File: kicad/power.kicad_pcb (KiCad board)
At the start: 2 copper layers, 84.1 x 61.7 mm, 10 parts, among them J1 Bus_PCI_Express_x1, J6 USB_C_Receptacle_USB2.0_16P, U1 MP2672GD-0000-Z, U3 MP2236CGJ-Z, U301 MR30-Vertical, U302 MP2236CGJ-Z

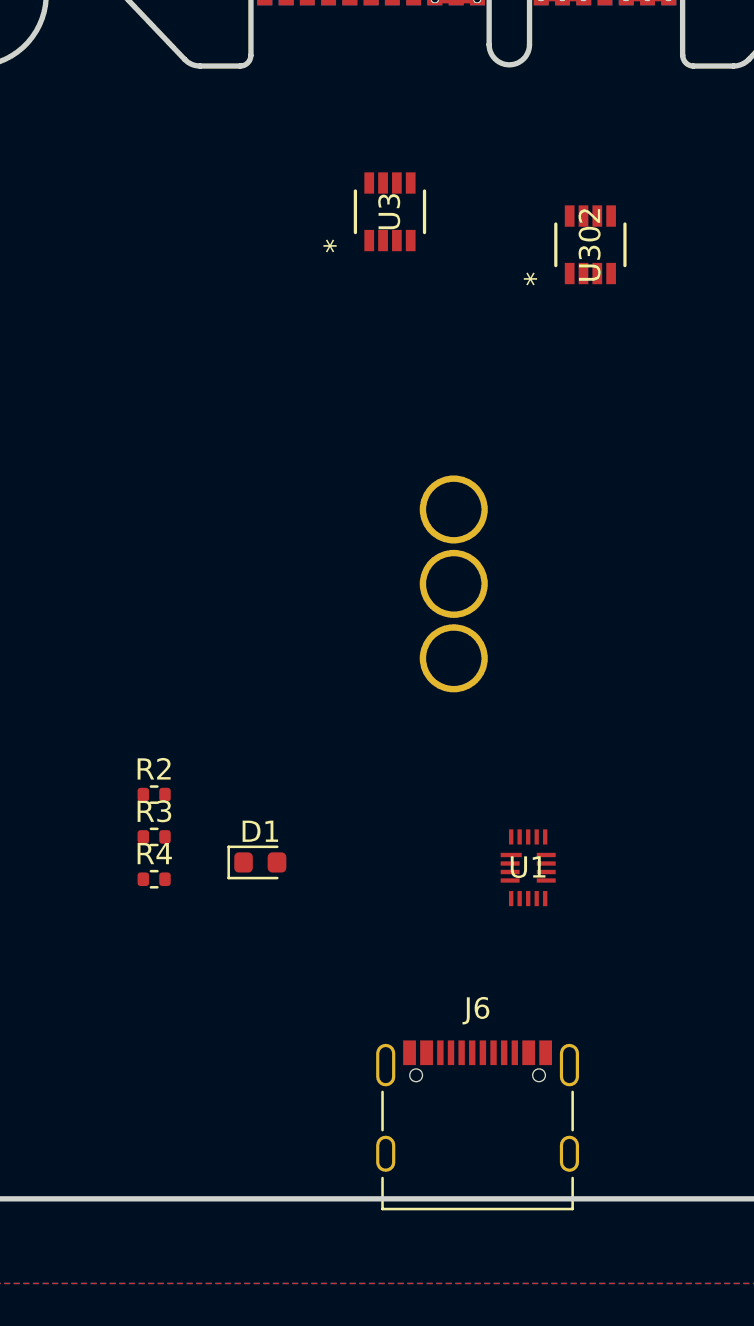
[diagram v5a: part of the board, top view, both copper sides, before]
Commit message: add LCSC PNs and footprints for various components, import custom step file for inductor
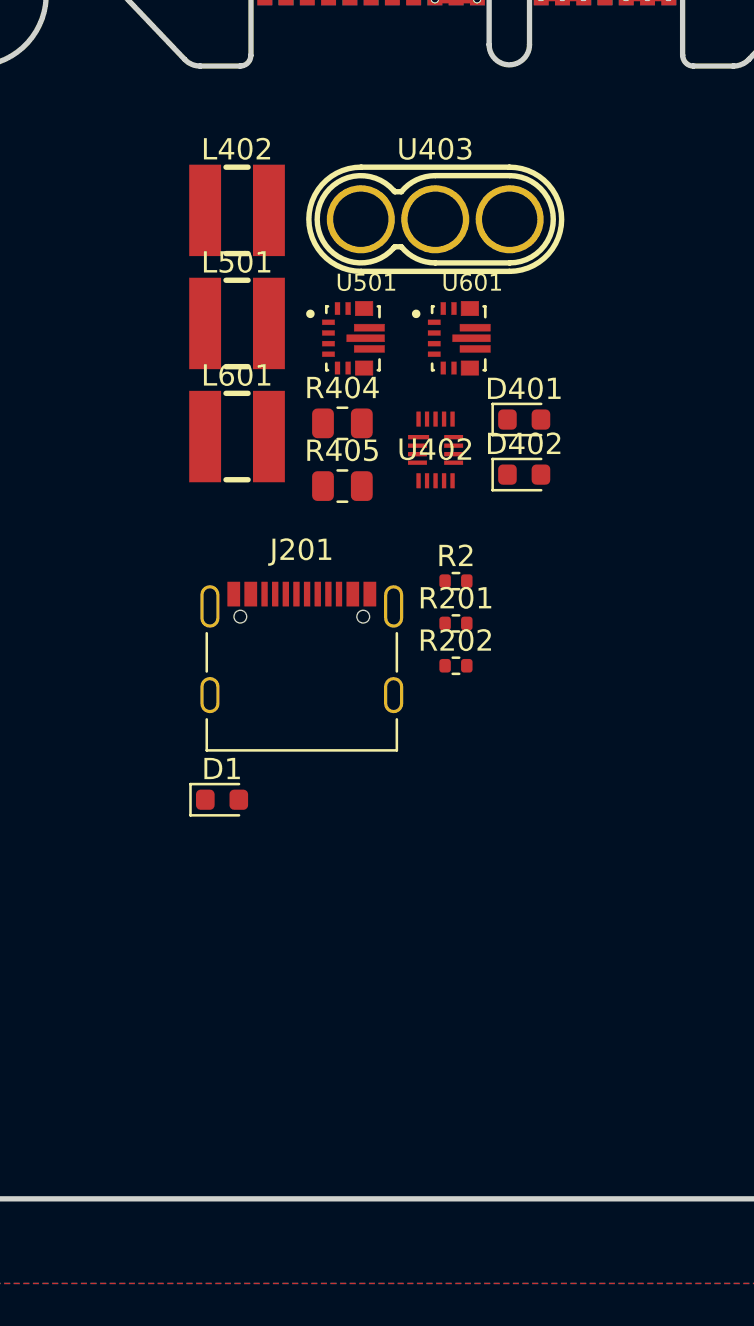
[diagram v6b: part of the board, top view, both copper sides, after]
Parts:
- removed J6: USB_C_Receptacle_USB2.0_16P, Connector_USB:USB_C_Receptacle_Palconn_UTC16-G
- removed R3, R4: 5.1k, Resistor_SMD:R_0402_1005Metric
- removed U1: MP2672GD-0000-Z, 4in-power:QFN-18_2MMx3MM_MP2672_MNP_MPS
- removed U3, U302: MP2236CGJ-Z, 4in-power:TSOT23-8_MP2236C_MNP
- removed U301: MR30-Vertical, 4in-power:CONN-TH_MR30-Vertical
- added D401: LED, LED_SMD:LED_0603_1608Metric, F.Cu at (149.1, 85.8)
- added D402: LED, LED_SMD:LED_0603_1608Metric, F.Cu at (149.1, 88.4)
- added J201: USB_C_Receptacle_USB2.0_16P, Connector_USB:USB_C_Receptacle_Palconn_UTC16-G, F.Cu at (138.7, 96.5)
- added L402: 1.5u, 4in-power:IND-SMD_L4.0-W4.0_YSMC0420V, F.Cu at (135.6, 75.9)
- added L501: 1.5u, 4in-power:IND-SMD_L4.0-W4.0_YSMC0420V, F.Cu at (135.6, 81.3)
- added L601: 1.5u, 4in-power:IND-SMD_L4.0-W4.0_YSMC0420V, F.Cu at (135.6, 86.6)
- added R201: 5.1k, Resistor_SMD:R_0402_1005Metric, F.Cu at (145.9, 95.4)
- added R202: 5.1k, Resistor_SMD:R_0402_1005Metric, F.Cu at (145.9, 97.3)
- added R404: 25k, Resistor_SMD:R_0805_2012Metric, F.Cu at (140.6, 85.9)
- added R405: 9.1k, Resistor_SMD:R_0805_2012Metric, F.Cu at (140.6, 88.9)
- added U402: MP2672GD-0000-Z, 4in-power:QFN-18_2MMx3MM_MP2672_MNP_MPS, F.Cu at (144.9, 87.2)
- added U403: Battery, 4in-power:CONN-TH_MR30-Vertical, F.Cu at (144.9, 76.4)
- added U501: TPS63070RNMR, 4in-power:VREG_TPS63070RNMR, F.Cu at (141.1, 81.9)
- added U601: TPS63070RNMR, 4in-power:VREG_TPS63070RNMR, F.Cu at (146.0, 81.9)
- moved R2 17.4 mm to (145.9, 93.4)
- moved D1 3.45 mm to (134.9, 103.6)

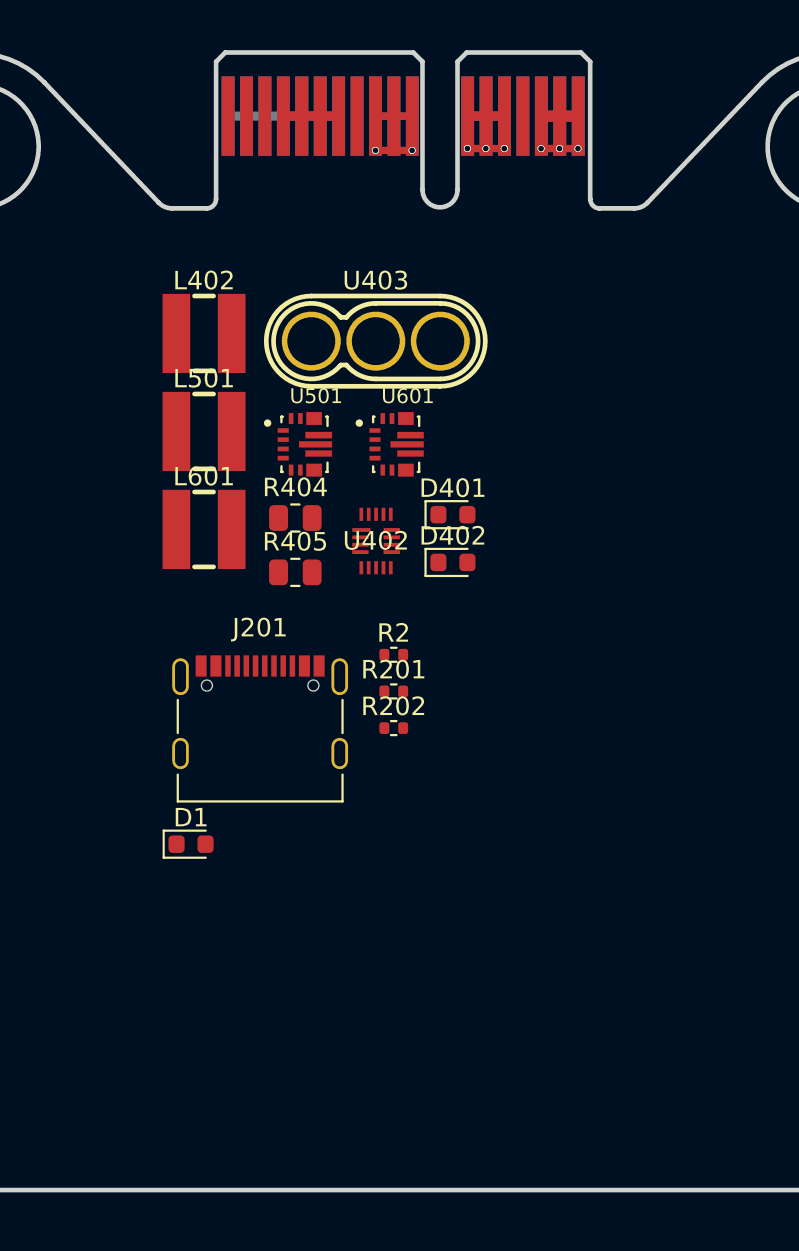
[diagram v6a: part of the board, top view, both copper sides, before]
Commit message: add all components to schematic
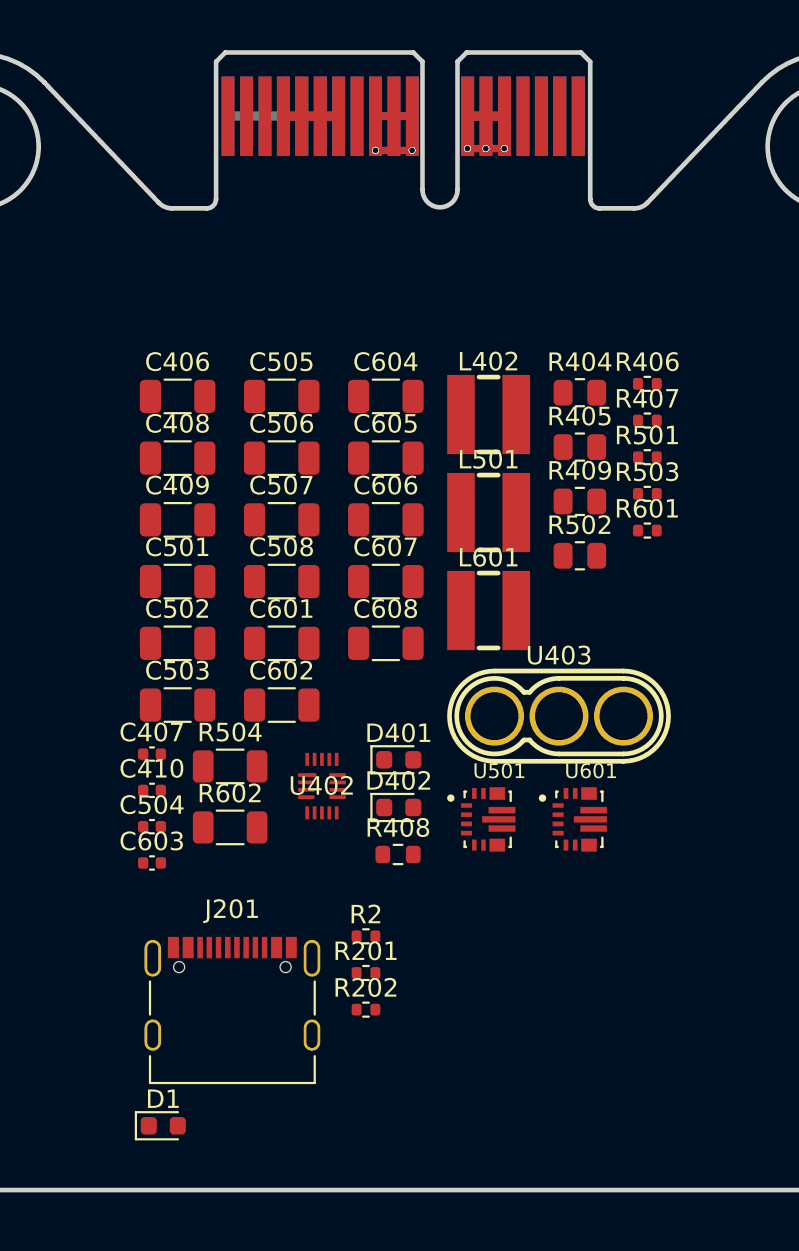
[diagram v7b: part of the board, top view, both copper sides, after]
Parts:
- added C406: 10u, Capacitor_SMD:C_1206_3216Metric, F.Cu at (134.2, 79.3)
- added C407: 100n, Capacitor_SMD:C_0402_1005Metric, F.Cu at (132.8, 98.8)
- added C408: 22u, Capacitor_SMD:C_1206_3216Metric, F.Cu at (134.2, 82.7)
- added C409: 22u, Capacitor_SMD:C_1206_3216Metric, F.Cu at (134.2, 86.0)
- added C410: 1u, Capacitor_SMD:C_0402_1005Metric, F.Cu at (132.8, 100.7)
- added C501: 10u, Capacitor_SMD:C_1206_3216Metric, F.Cu at (134.2, 89.4)
- added C502: 10u, Capacitor_SMD:C_1206_3216Metric, F.Cu at (134.2, 92.8)
- added C503: 10u, Capacitor_SMD:C_1206_3216Metric, F.Cu at (134.2, 96.1)
- added C504: 100n, Capacitor_SMD:C_0402_1005Metric, F.Cu at (132.8, 102.7)
- added C505: 10u, Capacitor_SMD:C_1206_3216Metric, F.Cu at (139.8, 79.3)
- added C506: 22u, Capacitor_SMD:C_1206_3216Metric, F.Cu at (139.8, 82.7)
- added C507: 22u, Capacitor_SMD:C_1206_3216Metric, F.Cu at (139.8, 86.0)
- added C508: 22u, Capacitor_SMD:C_1206_3216Metric, F.Cu at (139.8, 89.4)
- added C601: 10u, Capacitor_SMD:C_1206_3216Metric, F.Cu at (139.8, 92.8)
- added C602: 10u, Capacitor_SMD:C_1206_3216Metric, F.Cu at (139.8, 96.1)
- added C603: 100n, Capacitor_SMD:C_0402_1005Metric, F.Cu at (132.8, 104.7)
- added C604: 22u, Capacitor_SMD:C_1206_3216Metric, F.Cu at (145.5, 79.3)
- added C605: 22u, Capacitor_SMD:C_1206_3216Metric, F.Cu at (145.5, 82.7)
- added C606: 22u, Capacitor_SMD:C_1206_3216Metric, F.Cu at (145.5, 86.0)
- added C607: 10u, Capacitor_SMD:C_1206_3216Metric, F.Cu at (145.5, 89.4)
- added C608: 10u, Capacitor_SMD:C_1206_3216Metric, F.Cu at (145.5, 92.8)
- added R406: 1k, Resistor_SMD:R_0402_1005Metric, F.Cu at (159.7, 78.7)
- added R407: 1k, Resistor_SMD:R_0402_1005Metric, F.Cu at (159.7, 80.7)
- added R408: 33k, Resistor_SMD:R_0603_1608Metric, F.Cu at (146.1, 104.2)
- added R409: 6k, Resistor_SMD:R_0805_2012Metric, F.Cu at (156.0, 85.0)
- added R501: 10k, Resistor_SMD:R_0402_1005Metric, F.Cu at (159.7, 82.7)
- added R502: 470k, Resistor_SMD:R_0805_2012Metric, F.Cu at (156.0, 88.0)
- added R503: 150k, Resistor_SMD:R_0402_1005Metric, F.Cu at (159.7, 84.6)
- added R504: 100k, Resistor_SMD:R_1206_3216Metric, F.Cu at (137.0, 99.4)
- added R601: 10k, Resistor_SMD:R_0402_1005Metric, F.Cu at (159.7, 86.6)
- added R602: 100k, Resistor_SMD:R_1206_3216Metric, F.Cu at (137.0, 102.7)
- moved U501 22.6 mm to (151.0, 102.3)
- moved U601 22.6 mm to (156.0, 102.3)
- moved U403 22.6 mm to (154.9, 96.7)
- moved R405 16.9 mm to (156.0, 82.1)
- moved R404 16.9 mm to (156.0, 79.2)
- moved L402 16.1 mm to (151.1, 80.3)
- moved L501 16.1 mm to (151.1, 85.7)
- moved L601 16.1 mm to (151.1, 91.0)
- moved D1 15.4 mm to (133.4, 118.9)
- moved R2 15.4 mm to (144.4, 108.7)
- moved J201 15.4 mm to (137.1, 111.8)
- moved R201 15.4 mm to (144.4, 110.6)
- moved R202 15.4 mm to (144.4, 112.6)
- moved U402 13.6 mm to (142.0, 100.5)
- moved D401 13.6 mm to (146.2, 99.1)
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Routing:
- net (no net): track 6.00 -> 0.00 mm, vias 3 -> 0

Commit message: progress charging/balancing routing
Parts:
- removed R2: 1k, Resistor_SMD:R_0402_1005Metric
- added R11: 1k, Resistor_SMD:R_0402_1005Metric, F.Cu at (38.2, 97.5)
- U403: value Battery -> Battery (MR-30); moved to B.Cu
- moved D1 98.4 mm to (38.2, 93.9)
- moved R501 89.0 mm to (74.4, 57.3)
- moved R503 89.0 mm to (74.4, 59.3)
- moved R601 82.0 mm to (77.7, 88.6)
- moved L601 79.9 mm to (71.2, 93.3)
- moved R502 72.5 mm to (88.8, 60.7)
- moved L501 70.3 mm to (88.4, 53.7)
- moved C602 69.5 mm to (70.7, 103.3)
- moved C604 69.4 mm to (77.4, 92.9)
- moved C605 69.4 mm to (77.4, 96.2)
- moved C606 69.4 mm to (77.4, 99.6)
- moved C607 69.4 mm to (77.4, 103.0)
- moved C608 69.4 mm to (77.4, 106.3)
- moved C601 69.4 mm to (70.7, 98.5)
- moved C504 64.1 mm to (75.0, 74.9)
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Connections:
- C410 pad 2: Net-(U402-VCC) -> /power/VCC
- U402 pad 4: Net-(U402-VCC) -> /power/VCC
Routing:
- net /power/VSYS: track 0.00 -> 37.5 mm
- net /power/VCC: track 0.00 -> 36.0 mm, vias 0 -> 3
- net /VBUS: track 0.00 -> 32.8 mm
- net AGND: track 0.00 -> 21.1 mm, vias 0 -> 2
- net Net-(U402-*STAT): track 0.00 -> 16.1 mm
- net Net-(U402-BATT): track 0.00 -> 13.7 mm
- net Net-(U402-MID): track 0.00 -> 13.2 mm
- net Net-(D402-K): track 0.00 -> 11.1 mm
- net Net-(U402-*ACOK): track 0.00 -> 10.0 mm
- net Net-(C407-Pad1): track 0.00 -> 9.49 mm
- net Net-(D401-K): track 0.00 -> 8.19 mm
- net Net-(J201-CC1): track 0.00 -> 7.36 mm
- net Net-(J201-CC2): track 0.00 -> 6.49 mm
- net Net-(U402-VLIM): track 0.00 -> 5.60 mm
- net Net-(U402-ISET): track 0.00 -> 5.25 mm
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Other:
- board text added: "Charge"
- board text added: "ok?"
